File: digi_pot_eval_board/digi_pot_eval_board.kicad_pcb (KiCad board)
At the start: 2 copper layers, 110.5 x 160.7 mm, 78 parts, among them J1 Conn_01x07_Male, J10 Conn_01x02_Male, J13 Conn_01x06_Male, J2 Conn_01x10_Male, J3 47346-0001, J8 DS1013-06S, J9 Conn_01x05_Male, K2 G6K2FYTR5DC, K4 G6K2FYTR5DC, K5 G6K2FYTR5DC, K6 G6K2FYTR5DC, K7 G6K2FYTR5DC, Q1 BSS84, Q2 BSS84, SW3 SW_Push, U1 DigiPot, U10 6N138, U11 NCP1117ST50T3G, U12 ATmega32U4-AU, U2 DigiPot, U3 DigiPot, U4 DigiPot, U5 DigiPot, U6 DigiPot, U7 DigiPot, U8 ULN2003A, U9 USBLC6-2SC6, Y1 16MHz HC-49SM

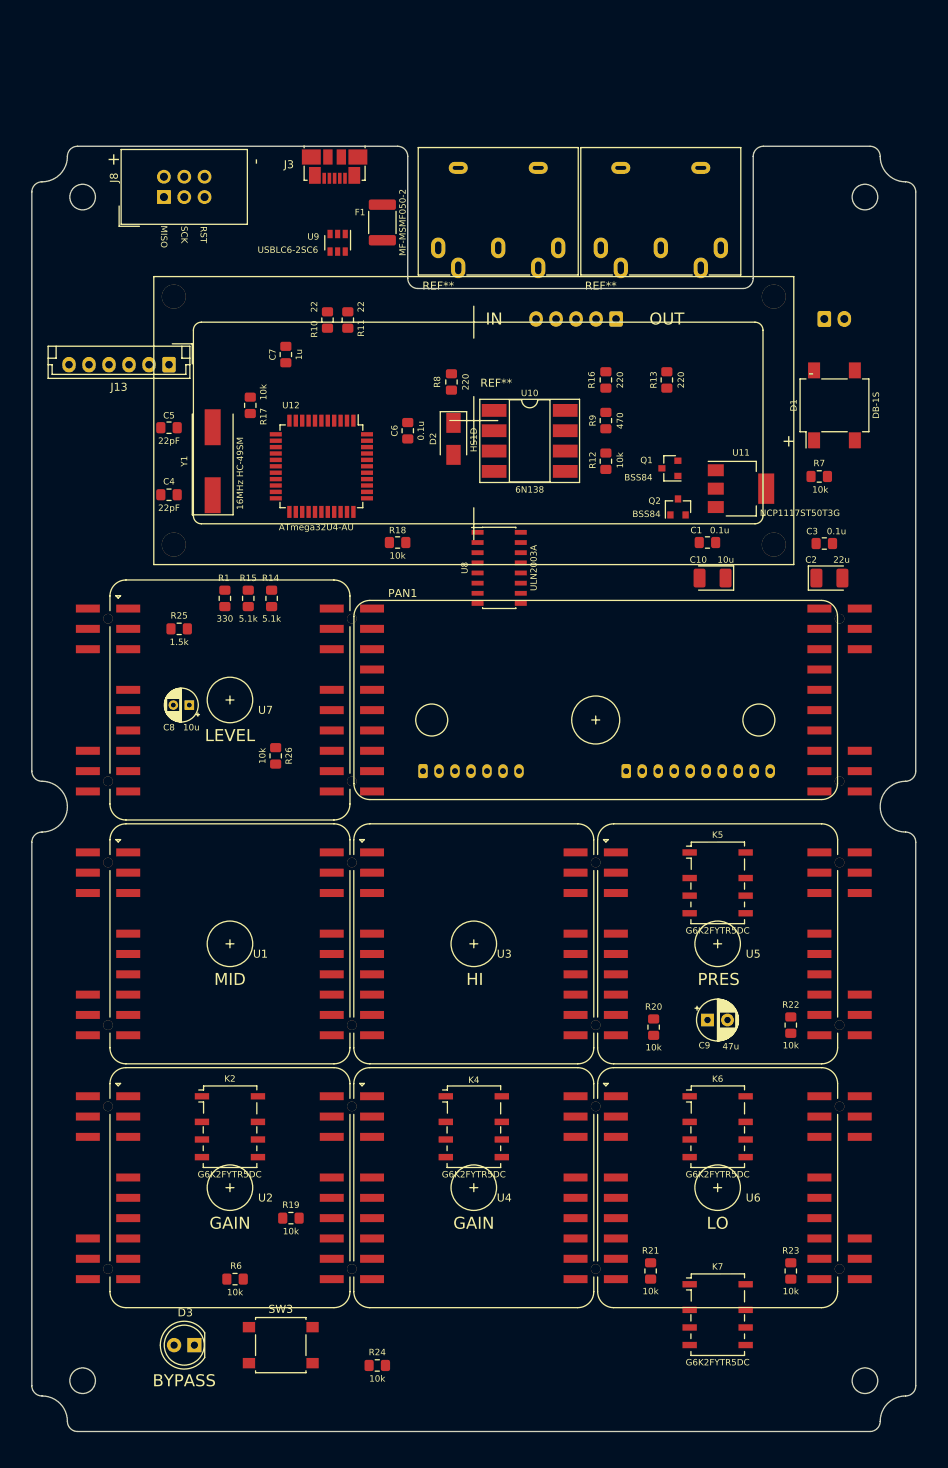
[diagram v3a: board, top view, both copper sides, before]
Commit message: Printed and tested layout version.
USB still on upper board.
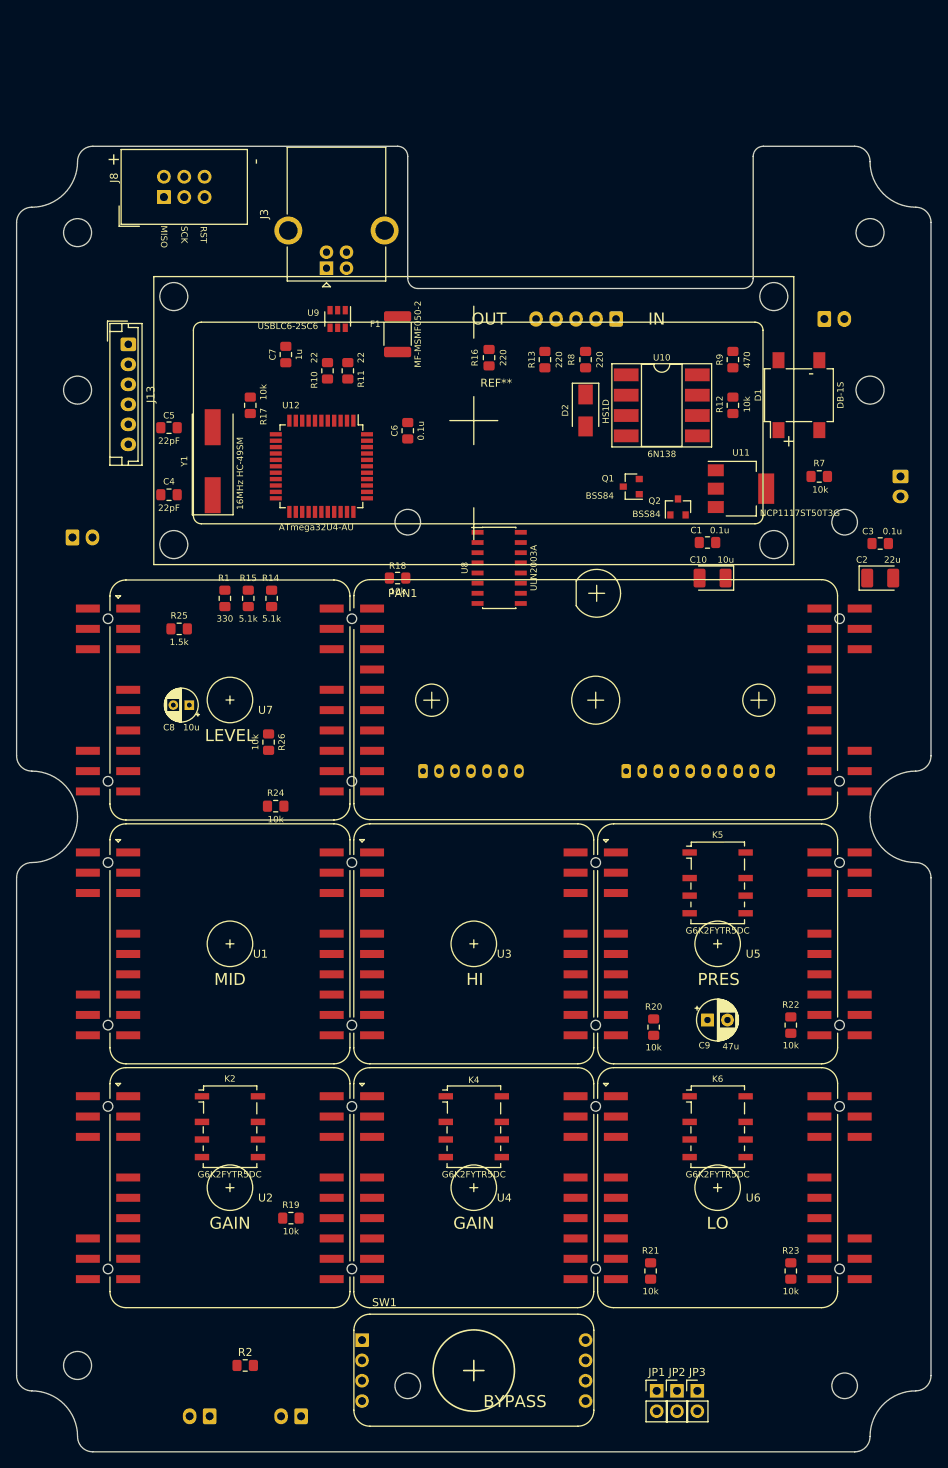
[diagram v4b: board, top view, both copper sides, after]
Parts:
- removed D3: LED, LED_THT:LED_D5.0mm
- removed K7: G6K2FYTR5DC, Relay_SMD:Relay_DPDT_Omron_G6K-2F-Y
- removed R6: 10k, Resistor_SMD:R_0805_2012Metric_Pad1.15x1.40mm_HandSolder
- removed the REF** at (131.4, 41.3)
- removed the REF** at (66.7, 182.9)
- removed the REF** at (164.5, 182.9)
- removed the REF** at (164.5, 34.9)
- removed the REF** at (66.7, 34.9)
- removed the REF** at (111.1, 41.3)
- removed SW3: SW_Push, Button_Switch_SMD:SW_SPST_B3S-1000
- added J11: Conn_01x02_Male, Connector_JST:JST_EH_B02B-EH-A_1x02_P2.50mm_Vertical, B.Cu at (82.5, 187.3)
- added J12: Conn_01x02_Male, Connector_JST:JST_EH_B02B-EH-A_1x02_P2.50mm_Vertical, B.Cu at (94.0, 187.3)
- added J4: Conn_01x02_Male, Connector_JST:JST_EH_B02B-EH-A_1x02_P2.50mm_Vertical, B.Cu at (65.4, 77.5)
- added J7: Conn_01x02_Male, Connector_JST:JST_EH_B02B-EH-A_1x02_P2.50mm_Vertical, B.Cu at (168.9, 69.8)
- added JP1: Jumper_NC_Small, Connector_PinHeader_2.54mm:PinHeader_1x02_P2.54mm_Vertical, F.Cu at (138.4, 184.2)
- added JP2: Jumper_NC_Small, Connector_PinHeader_2.54mm:PinHeader_1x02_P2.54mm_Vertical, F.Cu at (141.0, 184.2)
- added JP3: Jumper_NC_Small, Connector_PinHeader_2.54mm:PinHeader_1x02_P2.54mm_Vertical, F.Cu at (143.5, 184.2)
- added R2: 10k, Resistor_SMD:R_0805_2012Metric_Pad1.15x1.40mm_HandSolder, F.Cu at (87.0, 181.0)
- added REF**: MountingHole_3.5mm, MountingHole:MountingHole_3.5mm, F.Cu at (66.0, 181.0)
- added REF**: MountingHole_3.5mm, MountingHole:MountingHole_3.5mm, F.Cu at (165.1, 59.1)
- added REF**: MountingHole_3.5mm, MountingHole:MountingHole_3.5mm, F.Cu at (66.0, 59.1)
- added REF**: MountingHole_3.5mm, MountingHole:MountingHole_3.5mm, F.Cu at (66.0, 39.4)
- added REF**: , orig_pcb:pq-4, B.Cu at (134.6, 129.5)
- added REF**: MountingHole_3.5mm, MountingHole:MountingHole_3.5mm, F.Cu at (165.1, 39.4)
- added SW1: SW_MEC_5G_LED, bypass_panel:bypass_panel_THT, F.Cu at (101.6, 177.8)
- J3: value 47346-0001 -> USB_B; footprint Connector_USB:USB_Micro-B_Molex_47346-0001 -> Connector_USB:USB_B_OST_USB-B1HSxx_Horizontal
- moved R24 71.1 mm to (90.8, 111.1)
- moved R9 17.6 mm to (148.0, 55.2)
- moved R12 17.3 mm to (148.0, 61.0)
- moved U10 17.1 mm to (139.1, 61.0)
- moved R8 17.0 mm to (129.5, 55.2)
- moved D2 16.9 mm to (129.5, 61.6)
- moved R13 15.5 mm to (124.5, 55.2)
- moved R16 14.9 mm to (117.5, 55.0)
- moved F1 14.1 mm to (106.0, 52.1)
- moved J3 12.7 mm to (97.2, 43.8), turned to 90 degrees
- moved U9 9.52 mm to (98.6, 50.2)
- moved C3 6.99 mm to (166.4, 78.2)
- moved R10 6.35 mm to (97.3, 56.6)
- moved R11 6.35 mm to (99.8, 56.6)
- moved C2 6.35 mm to (166.4, 82.5)
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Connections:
- J3 pad 4: Net-(J3-Pad4) -> GND
- J9 pad 1: MOUT5 -> MIN5
- J9 pad 2: GND -> MIN4
- J9 pad 3: MOUT4 -> MOUT5
- J9 pad 4: MIN5 -> GND
- J9 pad 5: MIN4 -> MOUT4
- R1 pad 1: Net-(D3-Pad2) -> +5V
- R1 pad 2: PASSBACK_LED -> Net-(JP3-Pad2)
- U12 pad 25: SW_PASSBACK -> SW_BYPASS
- U12 pad 31: PASSBACK_LED -> BYPASS_LED
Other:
- board size 110.5 x 160.7 mm -> 114.3 x 163.2 mm

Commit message: Production version 2019.11.19.
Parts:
- added J14: Conn_01x02_Male, Connector_JST:JST_EH_B02B-EH-A_1x02_P2.50mm_Vertical, B.Cu at (168.9, 84.5)
- added REF**: KiCad-Logo2_5mm_SilkScreen, Symbol:KiCad-Logo2_5mm_SilkScreen, B.Cu at (146.7, 165.1)
- moved R1 120.5 mm to (151.1, 185.4), turned to 270 degrees
- moved R2 54.1 mm to (141.0, 177.2), turned to 90 degrees
- moved R21 15.6 mm to (122.6, 165.1), turned to 180 degrees
- moved F1 14.2 mm to (92.1, 49.5)
- moved R20 13.9 mm to (124.5, 135.9)
- moved C3 7.71 mm to (158.8, 79.4), turned to 270 degrees
- moved J10 7.24 mm to (166.4, 48.3), turned to 180 degrees
- moved R18 5.85 mm to (102.2, 78.1)
- moved R16 5.78 mm to (123.2, 55.9)
- moved R15 4.46 mm to (87.0, 80.6), turned to 180 degrees
- moved R24 4.43 mm to (91.4, 106.7)
- moved R13 3.86 mm to (128.3, 55.9)
- moved R23 3.18 mm to (152.4, 167.6), turned to 180 degrees
- moved C7 3.17 mm to (94.6, 56.5)
- moved Q1 3.17 mm to (132.1, 71.1)
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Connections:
- D1 pad 3: POW2 -> POW1
- D1 pad 4: POW1 -> POW2
- J13 pad 1: MOSI -> GND
- J13 pad 2: MISO -> +5V
- J13 pad 4: Net-(J13-Pad4) -> MISO
- J13 pad 5: +5V -> MOSI
- J13 pad 6: GND -> D_CS
- J4 pad 1: +5V -> KBP_SINK
- J4 pad 2: KBP_SINK -> +5V
- J7 pad 1: +9V -> GND
- J7 pad 2: GND -> +9V
- JP1 pad 1: BYPASS_LED -> BYP_L-
- JP1 pad 2: BYP_L- -> BYPASS_LED
- U12 pad 12: Net-(U12-Pad12) -> D_CS
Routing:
- net GND: track 0.00 -> 756.2 mm, vias 0 -> 28
- net +5V: track 0.00 -> 642.4 mm, vias 0 -> 31
- net SCL: track 0.00 -> 249.6 mm, vias 0 -> 11
- net SDA: track 0.00 -> 243.3 mm, vias 0 -> 12
- net CHG: track 0.00 -> 237.0 mm, vias 0 -> 8
- net C: track 0.00 -> 185.6 mm, vias 0 -> 14
- net SW_BYPASS: track 0.00 -> 168.5 mm, vias 0 -> 2
- net BYPASS_LED: track 0.00 -> 154.6 mm, vias 0 -> 3
- net A3: track 0.00 -> 140.6 mm, vias 0 -> 6
- net A1: track 0.00 -> 112.7 mm, vias 0 -> 4
- net L1: track 0.00 -> 98.5 mm, vias 0 -> 2
- net L3: track 0.00 -> 95.3 mm, vias 0 -> 2
- net KMW_SINK: track 0.00 -> 95.2 mm, vias 0 -> 2
- net KLW_SINK: track 0.00 -> 90.6 mm, vias 0 -> 2
- net SW_RIGHT: track 0.00 -> 90.3 mm, vias 0 -> 2
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- added copper zone on B.Cu, net GND
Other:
- board text added: "+5V"
- board text added: "+9V"
- board text added: "2019.11.18"
- board text added: "BYPASS BTN"
- board text added: "BYPASS LED"
- board text added: "BYPASS RELAY"
- board text added: "L- SW L+"
- board text added: "MIDI IN MIDI OUT"
- board text added: "POWER IN"
- board text added: "github.com/mar0x/pq-4"
